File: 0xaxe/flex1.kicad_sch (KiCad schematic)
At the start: 89 parts, among them U115 MCP1824T-1802E, U5001 25MHz, U5003 NCP114ASN080T1G, U5004 ADUM141E0BRZ-RL7, U5005 +0V8, U5006 +0V8, U5007 BM1366_mode1, U5008 +0V8, U5009 +0V8, U5010 +0V8, U5011 +0V8, U5012 +0V8, U5013 +0V8, U5014 +0V8, U5015 +0V8, U5016 +0V8, U5017 +0V8, U5018 BM1366_mode1, U5019 +0V8, U5020 +0V8, U5021 BM1366_mode1, U5022 +0V8, U5024 +0V8, U5025 BM1366_mode1, U5026 +0V8

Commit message: rev1.2
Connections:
- net +5V renamed +6.5V
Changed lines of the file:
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@@
 	)
 	(symbol
-		(lib_id "power:+5V")
-		(at 87.63 185.42 0)
-		(unit 1)
-		(exclude_from_sim no)
-		(in_bom yes)
-		(on_board yes)
-		(dnp no)
-		(fields_autoplaced yes)
-		(property "Reference" "#PWR0607"
-			(at 87.63 189.23 0)
-			(effects
-				(font
-					(size 1.27 1.27)
-				)
-				(hide yes)
-			)
-		)
-		(property "Value" "+5V"
-			(at 87.63 180.34 0)
-			(effects
-				(font
-					(size 1.27 1.27)
-				)
-			)
-		)
-		(property "Footprint" ""
-			(at 87.63 185.42 0)
-			(effects
-				(font
-					(size 1.27 1.27)
-				)
-				(hide yes)
-			)
-		)
-		(property "Datasheet" ""
-			(at 87.63 185.42 0)
-			(effects
-				(font
-					(size 1.27 1.27)
-				)
-				(hide yes)
-			)
-		)
-		(property "Description" "Power symbol creates a global label with name \"+5V\""
-			(at 87.63 185.42 0)
-			(effects
-				(font
-					(size 1.27 1.27)
-				)
-				(hide yes)
-			)
-		)
-		(pin "1"
-		)
-		(instances
-			(project "0xaxe"
-				(path "/e63e39d7-6ac0-4ffd-8aa3-1841a4541b55/84d407d0-bd71-403d-bc5c-679b63d0a5ac/3880e901-f61e-41a0-a16a-1a9a6a6176ec"
-					(reference "#PWR0607")
-					(unit 1)
-				)
-			)
-		)
-	)
-	(symbol
 		(lib_id "mylib7:+1V2_0")
 		(at 204.47 222.25 0)
@@
 					(unit 1)
 				)
+			)
+		)
+	)
+	(symbol
+		(lib_id "mylib7:+6.5V")
+		(at 87.63 185.42 0)
+		(unit 1)
+		(exclude_from_sim no)
+		(in_bom yes)
+		(on_board yes)
+		(dnp no)
+		(fields_autoplaced yes)
+		(property "Reference" "#PWR0491"
+			(at 87.63 189.23 0)
+			(effects
+				(font
+					(size 1.27 1.27)
+				)
+				(hide yes)
+			)
+		)
+		(property "Value" "+6.5V"
+			(at 87.63 180.34 0)
+			(effects
+				(font
+					(size 1.27 1.27)
+				)
+			)
+		)
+		(property "Footprint" ""
+			(at 87.63 185.42 0)
+			(effects
+				(font
+					(size 1.27 1.27)
+				)
+				(hide yes)
+			)
+		)
+		(property "Datasheet" ""
+			(at 87.63 185.42 0)
+			(effects
+				(font
+					(size 1.27 1.27)
+				)
+				(hide yes)
+			)
+		)
+		(property "Description" ""
+			(at 87.63 185.42 0)
+			(effects
+				(font
+					(size 1.27 1.27)
+				)
+				(hide yes)
+			)
+		)
+		(pin "1"
+		)
+		(instances
+			(project "0xaxe"
+				(path "/e63e39d7-6ac0-4ffd-8aa3-1841a4541b55/84d407d0-bd71-403d-bc5c-679b63d0a5ac/3880e901-f61e-41a0-a16a-1a9a6a6176ec"
+					(reference "#PWR0491")
+					(unit 1)
+				)

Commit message: op levelshifter
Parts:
- removed C5010, C5011: 100n, Capacitor_SMD:C_0805_2012Metric, symbol Device:C
- removed U5004: ADUM141E0BRZ-RL7, Package_SO:SOIC-16_3.9x9.9mm_P1.27mm, symbol Isolator:ADuM1411
- added C278, C281, C282, C283: 100pF, Capacitor_SMD:C_0805_2012Metric, symbol Device:C
- added C47: 0.1uF, Capacitor_SMD:C_0805_2012Metric, symbol Device:C
- added C48: 1uF, Capacitor_SMD:C_0805_2012Metric, symbol Device:C
- added R36, R43, R54, R55, R62, R65, R68, R69, R70: 1k, Resistor_SMD:R_0805_2012Metric, symbol Device:R
- added R37, R42, R48, R49, R63, R64, R66, R67: 10k, Resistor_SMD:R_0805_2012Metric, symbol Device:R
- added U16: TLV3544, Package_SO:SOIC-14_3.9x8.7mm_P1.27mm, symbol bitaxe:TLV3544
- renumbered C5002 to C39, C5003 to C40, C5004 to C41, C5005 to C42, C5006 to C43, C5007 to C44, C5009 to C46, C5012 to C49, C5013 to C50, C5014 to C51, C5015 to C52, C5016 to C53, C5017 to C54, C5018 to C55, C5019 to C56, C5020 to C57, C5021 to C58, C5022 to C59, C5023 to C60, C5024 to C61, C5025 to C62, C5026 to C63, C5027 to C64, C5028 to C65, C5029 to C66, C5030 to C67, C5031 to C68, C5032 to C69, C5033 to C70, C5034 to C71, C5035 to C72, C5036 to C73, C5037 to C74, C5038 to C75, C5039 to C76, C5040 to C77, C5041 to C78, C5042 to C79, C5043 to C80, C5044 to C81, C5045 to C82, C5046 to C83, C5047 to C84, C5048 to C85, C5049 to C86, C5050 to C87, C5051 to C88, C5052 to C89, C5053 to C90, C5054 to C91, C5055 to C92, C5057 to C93, C5058 to C94, C5059 to C95, C5060 to C96, C5061 to C97, R5003 to R38, R5004 to R39, R5005 to R40, R5006 to R41, U5001 to U13, U5003 to U15, U5005 to U17, U5006 to U18, U5007 to U19, U5008 to U20, U5009 to U21, U5010 to U22, U5011 to U23, U5012 to U24, U5013 to U25, U5014 to U26, U5015 to U27, U5016 to U28, U5017 to U29, U5018 to U30, U5019 to U31, U5020 to U32, U5021 to U33, U5022 to U34, U5024 to U35, U5025 to U36, U5026 to U37
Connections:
- net +6.5V: now also C47.2, C48.2, U16.4 (V+)
- net BI: now also R67.1
- net CI: now also R42.1
- net NRSTI: now also R49.1
- net NRSTO: now also C281.2, R55.1, U16.7; no longer U19.5 (NRSTI)
- net RO: now also R70.1
- net CLKI renamed I_CLKI
- new net: R66.2, R67.2, U16.10 (+)
- new net: C283.1, R65.1, R69.2, U16.9 (-)
- new net: C282.1, R62.1, R68.2, U16.13 (-)
- new net: C282.2, R68.1, R70.2, U16.14
- new net: R48.2, R49.2, U16.5 (+)
- new net: C278.1, R36.1, R54.2, U16.2 (-)
- new net: R37.1, R42.2, U16.3 (+)
- new net: R63.2, R64.2, U16.12 (+)
- new net: C281.1, R43.1, R55.2, U16.6 (-)
- new net -VDD_1: R63.1
- new net BI_1: C283.2, R69.1, U16.8
- new net CI_1: C278.2, R54.1, U16.1
- new net GND: C47.1, C48.1, U16.11 (V-)
- new net GND_1: R36.2, R43.2, R62.2, R65.2
- new net I_NRSTI: U19.5 (NRSTI)
- new net RO_1: R64.1
- new net VDD_1: R37.2, R48.1, R66.1
- no-connect marks 21 -> 19
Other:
- note added: "+0V8 LDO"
- note added: "+1V8 LDO"
- note added: "25MHz Osc for CLKI"
- note added: "Levelshift of input signals to own voltage domain"
- note added: "OPAMP Bypass"
- moved on the sheet: C279, C280, C39, C40, C43, C50, C51, C53, C54, C55, C56, C58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

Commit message: General Update
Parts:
- U17, U18, U20, U21, U22, U23, U24, U25, U26, U27, U28, U29, U31, U32, U34, U35, U37: value +0V8 -> +0V8_0
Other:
- note added: "+0V8_0 LDO"
- note removed: "+0V8 LDO"
- moved on the sheet: C41, C42, C44, C46, C49, C50, C51, C52, C53, C54, C55, C56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

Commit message: fixed couple of things
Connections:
- net I_BI is gone; now on net I_BI_0: U19.6 (BI)
- net I_CI is gone; now on net I_CI_0: U19.9 (CI)
- net NRSTO is gone; now on net I_NRSTI_0: C281.2, R55.1, U16.7
- net RO_1 is gone; now on net I_RO_0: R64.1
- net -VDD_1 renamed VDD_REF_I_0
- net BI renamed BI_0
- net BI_1 renamed I_BI_0
- net BO: no longer names the net of U36.23 (BO)
- net CI renamed CI_0
- net CI_1 renamed I_CI_0
- net CO: no longer names the net of U36.20 (CO)
- net I_CLKI renamed I_CLKI_0
- net I_NRSTI renamed I_NRSTI_0
- net I_RO renamed I_RO_0
- net NRSTI renamed NRSTI_0
- net RI: no longer names the net of R41.1, U36.22 (RI)
- net RO renamed RO_0
- no-connect marks 19 -> 21
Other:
- moved on the sheet: C279, C280, C282, C283, C40, C41, C42, C43, C44, C46, C47, C48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

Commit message: Layout update
Layout with OP
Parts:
- removed R36, R43, R54, R55, R62, R65, R68, R69, R70: 1k, Resistor_SMD:R_0805_2012Metric, symbol Device:R
- removed R37, R42, R48, R49, R63, R64, R66, R67: 10k, Resistor_SMD:R_0805_2012Metric, symbol Device:R
- added RN1, RN2, RN3, RN4: 10k, EXB-28V103JX:EXB28V_PAN, symbol Device:R_Network04_Split
- U19, U30, U33, U36: footprint qaxe:BM1366 -> bitvein:BM1366
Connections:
- net +1V2_0: now also RN1.7 (R2.2), RN2.1 (R1), RN4.4 (R2.2)
- net BI_0: now also RN4.5 (R2.2)
- net CI_0: now also RN1.2 (R1.2)
- net GND_0: now also RN1.5 (R2.2), RN2.4 (R2.2), RN3.4 (R2.2), RN4.1 (R1)
- net I_BI_0: now also RN4.8 (R4.2)
- net I_CI_0: now also RN1.4 (R2.2)
- net I_NRSTI_0: now also RN2.5 (R2.2)
- net I_RO_0: now also RN3.8 (R4.2)
- net NRSTI_0: now also RN2.8 (R4.2)
- net RO_0: now also C282.2, U16.14, RN3.5 (R2.2)
- net VDD_REF_I_0: now also RN3.1 (R1)
- net at U16.10 (+): now also RN4.3 (R2.2), RN4.6 (R3.2)
- net at C283.1, U16.9 (-): now also RN4.2 (R1.2), RN4.7 (R2.2)
- net at C282.1, U16.13 (-): now also RN3.3 (R2.2), RN3.6 (R3.2)
- net at U16.5 (+): now also RN2.2 (R1.2), RN2.7 (R2.2)
- net at C278.1, U16.2 (-): now also RN1.3 (R2.2), RN1.6 (R3.2)
- net at U16.3 (+): now also RN1.1 (R1), RN1.8 (R4.2)
- net at U16.12 (+): now also RN3.2 (R1.2), RN3.7 (R2.2)
- net at C281.1, U16.6 (-): now also RN2.3 (R2.2), RN2.6 (R3.2)

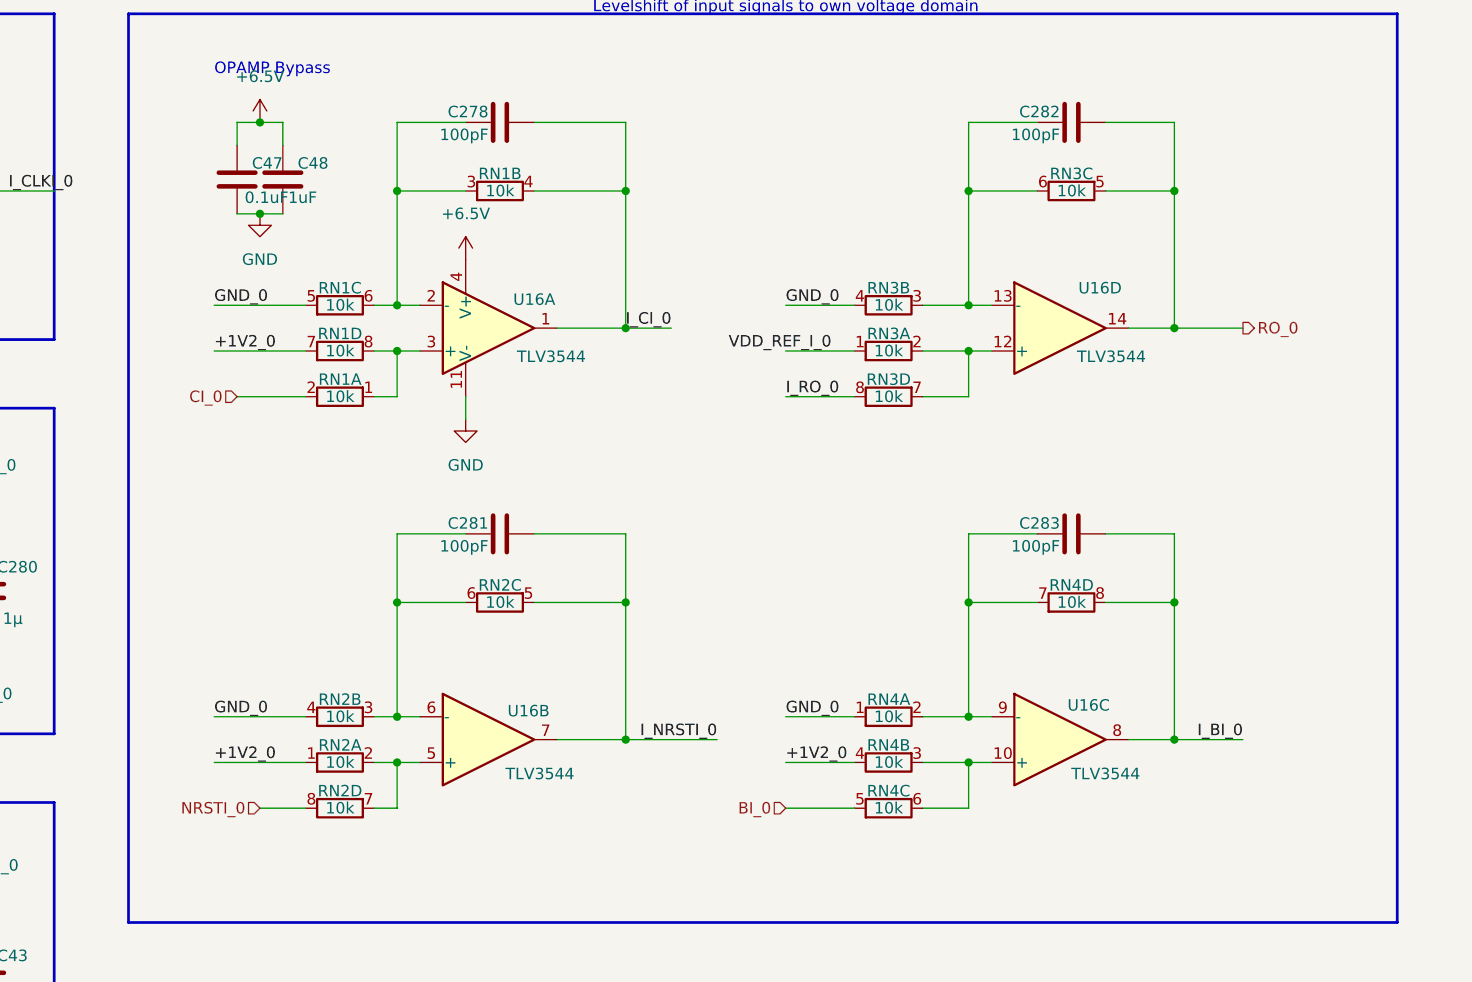
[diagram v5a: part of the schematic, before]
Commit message: fixed level shifter, added optional headers for future extensions
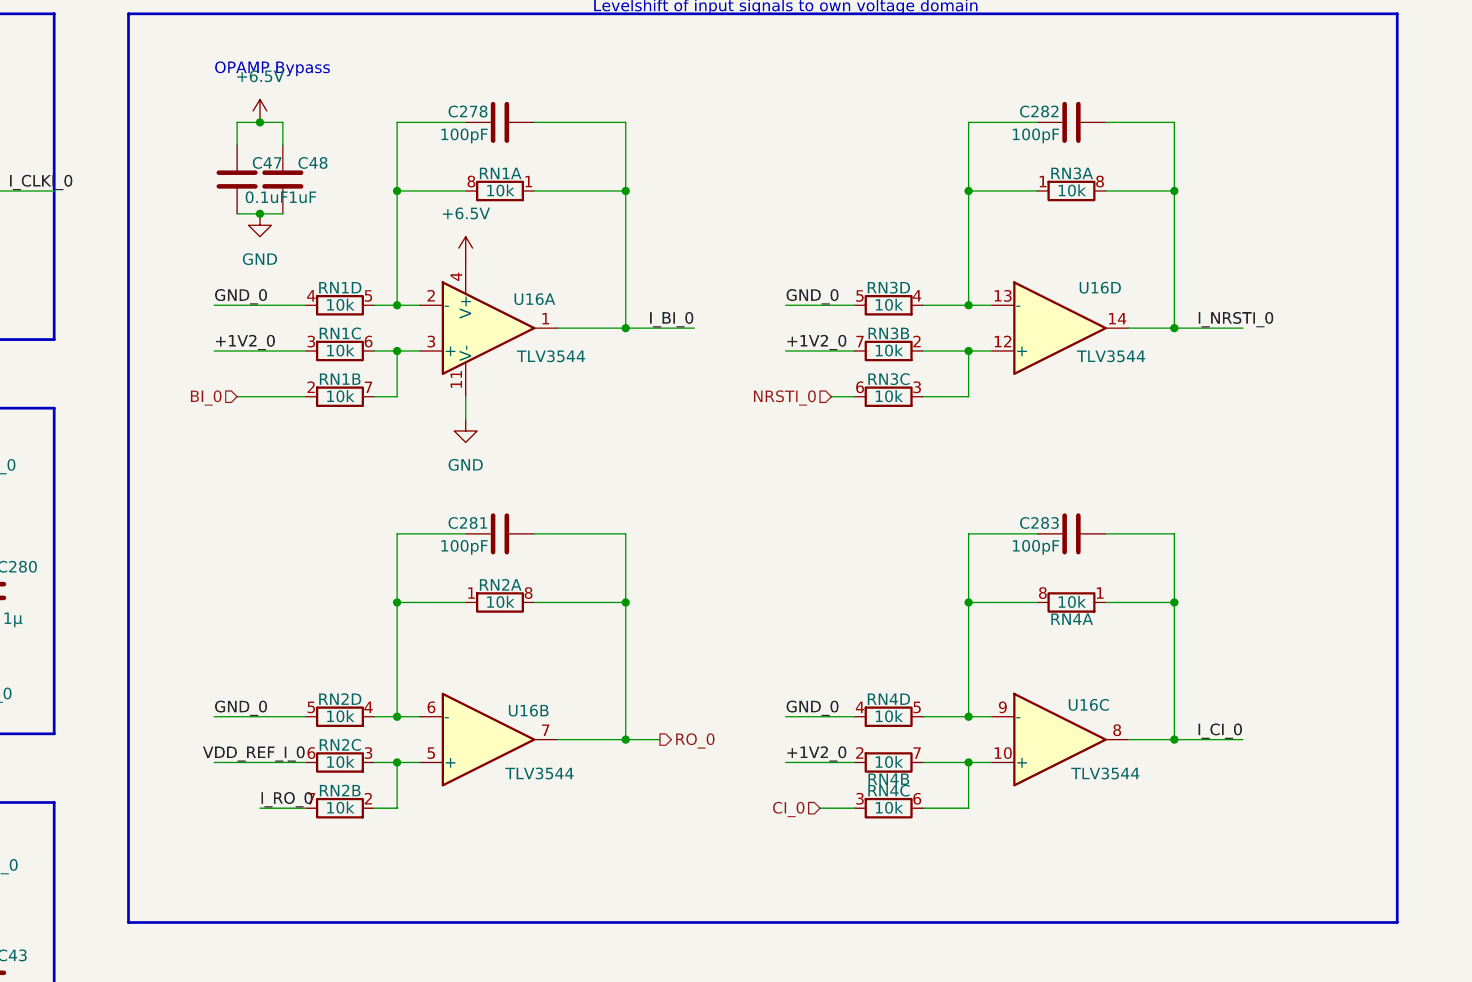
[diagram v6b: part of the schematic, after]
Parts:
- RN1, RN2, RN3, RN4: footprint EXB-28V103JX:EXB28V_PAN -> Resistor_SMD:R_Array_Convex_4x0603; symbol Device:R_Network04_Split -> mylib7:R_Network04_Split_SMD
- U19, U30, U33, U36: footprint bitvein:BM1366 -> myfootprints:BM1366-user1-soldermask
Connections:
- net +1V2_0: now also RN1.3 (R3.1), RN3.7 (R2.2), RN4.2 (R2.1); no longer RN1.7 (R2.2), RN2.1 (R1), RN4.4 (R2.2)
- net BI_0: now also RN1.2 (R2.1); no longer RN4.5 (R2.2)
- net CI_0: now also RN4.3 (R3.1); no longer RN1.2 (R1.2)
- net GND_0: now also RN1.4 (R4.1), RN2.5 (R4.2), RN3.5 (R4.2), RN4.4 (R4.1); no longer RN1.5 (R2.2), RN2.4 (R2.2), RN3.4 (R2.2), RN4.1 (R1)
- net I_BI_0: now also C278.2, RN1.1 (R1.1), U16.1; no longer C283.2, RN4.8 (R4.2), U16.8
- net I_CI_0: now also C283.2, RN4.1 (R1.1), U16.8; no longer C278.2, RN1.4 (R2.2), U16.1
- net I_NRSTI_0: now also C282.2, RN3.8 (R1.2), U16.14; no longer C281.2, RN2.5 (R2.2), U16.7
- net I_RO_0: now also RN2.7 (R2.2); no longer RN3.8 (R4.2)
- net NRSTI_0: now also RN3.6 (R3.2); no longer RN2.8 (R4.2)
- net RO_0: now also C281.2, RN2.8 (R1.2), U16.7; no longer C282.2, RN3.5 (R2.2), U16.14
- net VDD_REF_I_0: now also RN2.6 (R3.2); no longer RN3.1 (R1)
- net at RN4.6 (R3.2), U16.10 (+): now also RN4.7 (R2.2); no longer RN4.3 (R2.2)
- net at C283.1, U16.9 (-): now also RN4.5 (R4.2), RN4.8 (R1.2); no longer RN4.2 (R1.2), RN4.7 (R2.2)
- net at C282.1, U16.13 (-): now also RN3.1 (R1.1), RN3.4 (R4.1); no longer RN3.3 (R2.2), RN3.6 (R3.2)
- net at C281.1, U16.6 (-): now also RN2.1 (R1.1), RN2.4 (R4.1); no longer RN2.3 (R2.2), RN2.6 (R3.2)
- net at C278.1, U16.2 (-): now also RN1.5 (R4.2), RN1.8 (R1.2); no longer RN1.3 (R2.2), RN1.6 (R3.2)
- new net: RN2.2 (R2.1), RN2.3 (R3.1), U16.5 (+)
- new net: RN1.6 (R3.2), RN1.7 (R2.2), U16.3 (+)
- new net: RN3.2 (R2.1), RN3.3 (R3.1), U16.12 (+)
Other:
- moved on the sheet: RN1A, RN1B, RN1C, RN1D, RN2A, RN2B, RN2C, RN2D, RN3A, RN3B, RN3C, RN3D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

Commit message: updated BOM and gerbers
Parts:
- C278, C281, C282, C283: value 100pF -> 100p
- C47: value 0.1uF -> 100n
- C48: value 1uF -> 1µ
- RN1, RN2, RN3, RN4: value 10k -> 10k-CX; Distributor (none) -> D; Manufacturer (none) -> CAY16-1002F4LF; OrderNr (none) -> CAY16-1002F4LFCT-ND
- U16: value TLV3544 -> TLV9154; Distributor (none) -> D; Manufacturer (none) -> TLV9154IDR; OrderNr (none) -> 296-TLV9154IDRCT-ND
